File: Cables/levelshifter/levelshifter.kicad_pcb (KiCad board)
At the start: 2 copper layers, 40 x 18.5 mm, 55 parts, among them J1 DB25_Male, J10 Conn_01x01, J12 Conn_01x01, J13 Conn_01x01, J14 Conn_01x01, J15 Conn_01x01, J16 Conn_01x01, J17 Conn_01x01, J19 Conn_01x01, J2 Conn_01x01, J20 Conn_01x01, J21 Conn_01x01, J22 Conn_01x01, J23 Conn_01x01, J24 Conn_01x01, J25 Conn_01x01, J26 Conn_01x01, J27 Conn_01x01, J28 Conn_01x01, J29 Conn_01x01, J3 Conn_01x01, J4 Conn_01x01, J5 Conn_01x01, J6 Conn_01x01, J7 Conn_01x01, J9 Conn_01x01, U1 74AHCT1G126, U10 74AHCT1G125, U11 74AHCT1G125, U12 74AHCT1G125, U13 74AHCT1G125, U14 74AHCT1G126, U15 74AHCT1G126, U16 74AHCT1G126, U17 74AHCT1G126, U18 74AHCT1G126, U19 74AHCT1G126, U2 74AHCT1G126, U20 74AHCT1G126, U21 74AHCT1G125, U22 74AHCT1G125, U23 74AHCT1G125, U24 74AHCT1G125, U25 74AHCT1G125, U26 74AHCT1G125, U27 74AHCT1G126, U28 74AHCT1G125, U3 74AHCT1G126, U4 74AHCT1G126, U5 74AHCT1G126, U6 74AHCT1G126, U7 74AHCT1G126, U8 74AHCT1G125, U9 74AHCT1G125

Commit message: Tweak PT & LS PCBs
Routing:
- net /VOUT: track 84.6 -> 85.3 mm
- net /GND: vias 33 -> 34

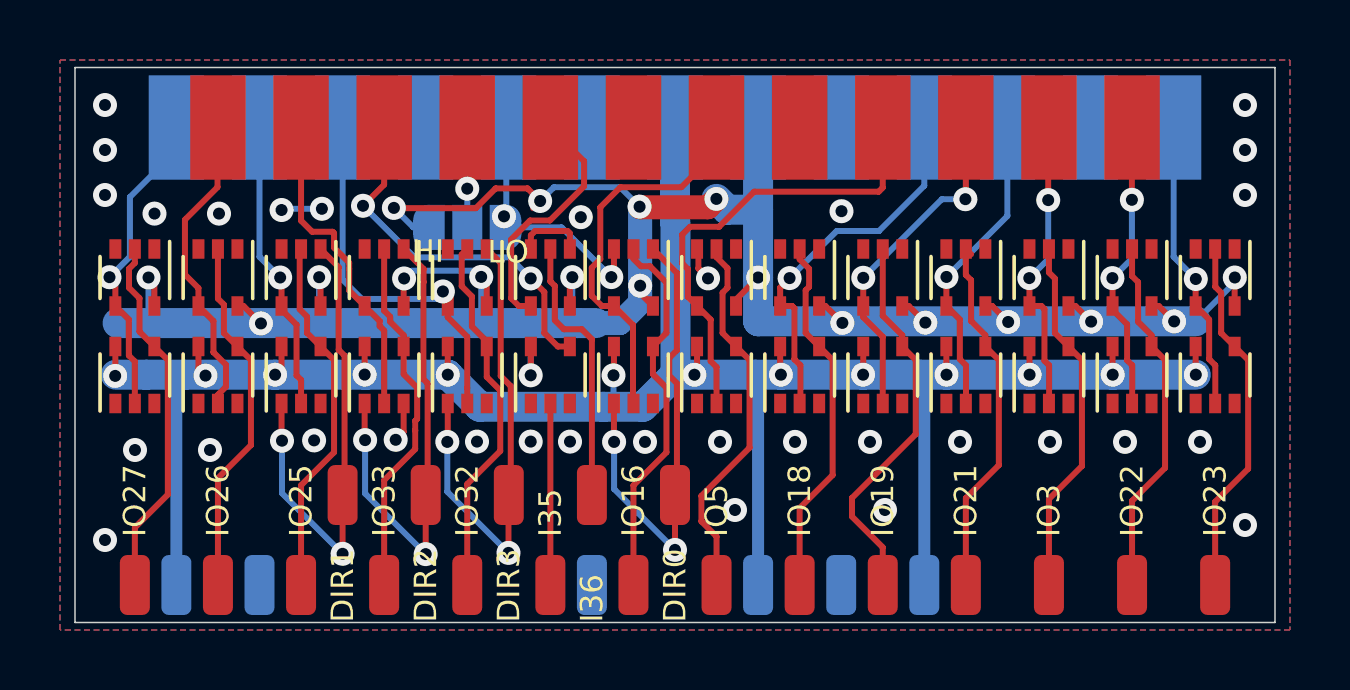
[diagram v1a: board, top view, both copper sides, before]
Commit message: Fixup inverted DB25 for Level Shifter PCB
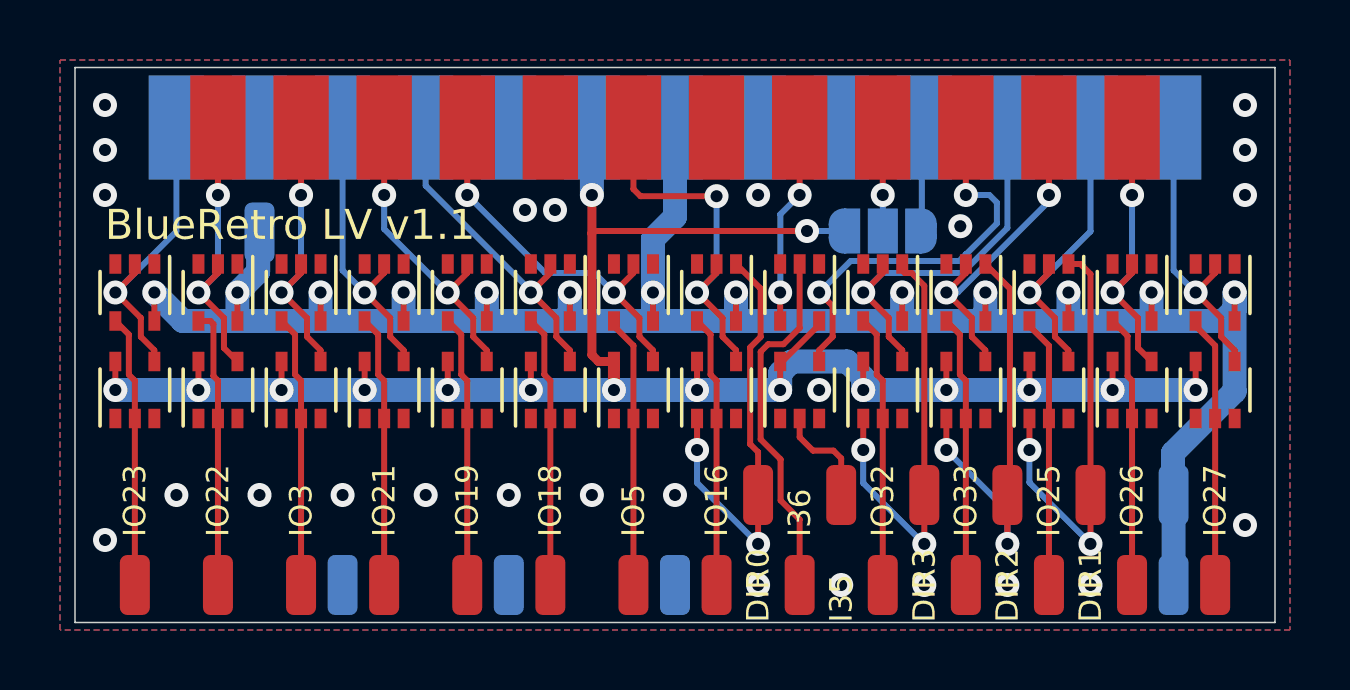
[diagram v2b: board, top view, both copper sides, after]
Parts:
- moved U1 36.2 mm to (-18.0, 1.50), turned to 90 degrees
- moved U18 36.2 mm to (18.0, 1.50), turned to 90 degrees
- moved U25 36.1 mm to (18.0, -1.75), turned to 270 degrees
- moved U8 36.1 mm to (-18.0, -1.75), turned to 270 degrees
- moved J29 36.0 mm to (18.0, 8.00)
- moved J9 36.0 mm to (-18.0, 8.00)
- moved J6 33.2 mm to (16.6, 8.00)
- moved U17 30.7 mm to (15.2, 1.50), turned to 90 degrees
- moved U2 30.7 mm to (-15.2, 1.50), turned to 90 degrees
- moved U24 30.6 mm to (15.2, -1.75), turned to 270 degrees
- moved U9 30.6 mm to (-15.2, -1.75), turned to 270 degrees
- moved J10 30.5 mm to (-15.2, 8.00)
- moved J28 30.5 mm to (15.2, 8.00)
- moved U15 25.2 mm to (12.5, 1.50), turned to 90 degrees
- moved U3 25.2 mm to (-12.5, 1.50), turned to 90 degrees
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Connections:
- J1 pad 1: /IO27 -> /IO23
- J1 pad 10: /IO18 -> /GND
- J1 pad 11: /IO21 -> /IO32
- J1 pad 12: (no net) -> /IO25
- J1 pad 13: /IO23 -> /IO27
- J1 pad 14: /IO26 -> /IO22
- J1 pad 15: /IO33 -> /IO3
- J1 pad 16: /I35 -> /IO19
- J1 pad 17: /I39 -> /IO5
- J1 pad 18: /I36 -> (no net)
- J1 pad 19: (no net) -> /IO16
- J1 pad 2: /IO25 -> (no net)
- J1 pad 20: /IO16 -> (no net)
- J1 pad 21: (no net) -> /I36
- J1 pad 22: /IO5 -> /I39
- J1 pad 23: /IO19 -> /I35
- J1 pad 24: /IO3 -> /IO33
- J1 pad 25: /IO22 -> /IO26
- J1 pad 3: /IO32 -> /IO21
- J1 pad 4: (no net) -> /IO18
- J1 pad 6: /GND -> /VOUT
- J1 pad 8: /VOUT -> /GND
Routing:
- net /VOUT: track 85.3 -> 69.4 mm, vias 19 -> 16
- net /GND: track 15.0 -> 3.49 mm, vias 34 -> 25
- net /IO19_C: track 13.0 -> 9.07 mm
- net /IO16_C: track 12.7 -> 9.07 mm
- net /IO5_C: track 12.7 -> 9.07 mm
- net /IO21_C: track 12.4 -> 9.07 mm
- net /IO27_C: track 12.3 -> 9.07 mm
- net /IO32_C: track 12.3 -> 9.07 mm
- net /IO18_C: track 12.2 -> 9.07 mm
- net /IO25_C: track 12.1 -> 9.07 mm
- net /IO33_C: track 12.1 -> 9.07 mm
- net /IO23_C: track 12.1 -> 9.07 mm
- net /IO3_C: track 12.1 -> 9.07 mm
- net /IO26_C: track 12.1 -> 9.07 mm
- net /I36_C: track 9.13 -> 12.1 mm
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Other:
- board text added: "BlueRetro LV v1.1"
- board text removed: "BlueRetro LV v1.0"

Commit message: Final tweak for JVS & LS PCBs
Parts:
- added J8: Conn_01x01, levelshifter:SolderWirePad_1x01_SMD_1x2mm, F.Cu at (16.6, 5.00)
- moved J6 3.30 mm to (15.2, 5.00)
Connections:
- U18 pad 1: /GND -> /DIR4
- U25 pad 1: /GND -> /DIR4
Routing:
- net /DIR4: track 0.00 -> 12.9 mm
- net /VIN: track 79.1 -> 77.5 mm
- net /GND: vias 25 -> 27
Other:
- board text added: "BlueRetro LS v1.1"
- board text added: "DIR4"
- board text removed: "BlueRetro LV v1.1"

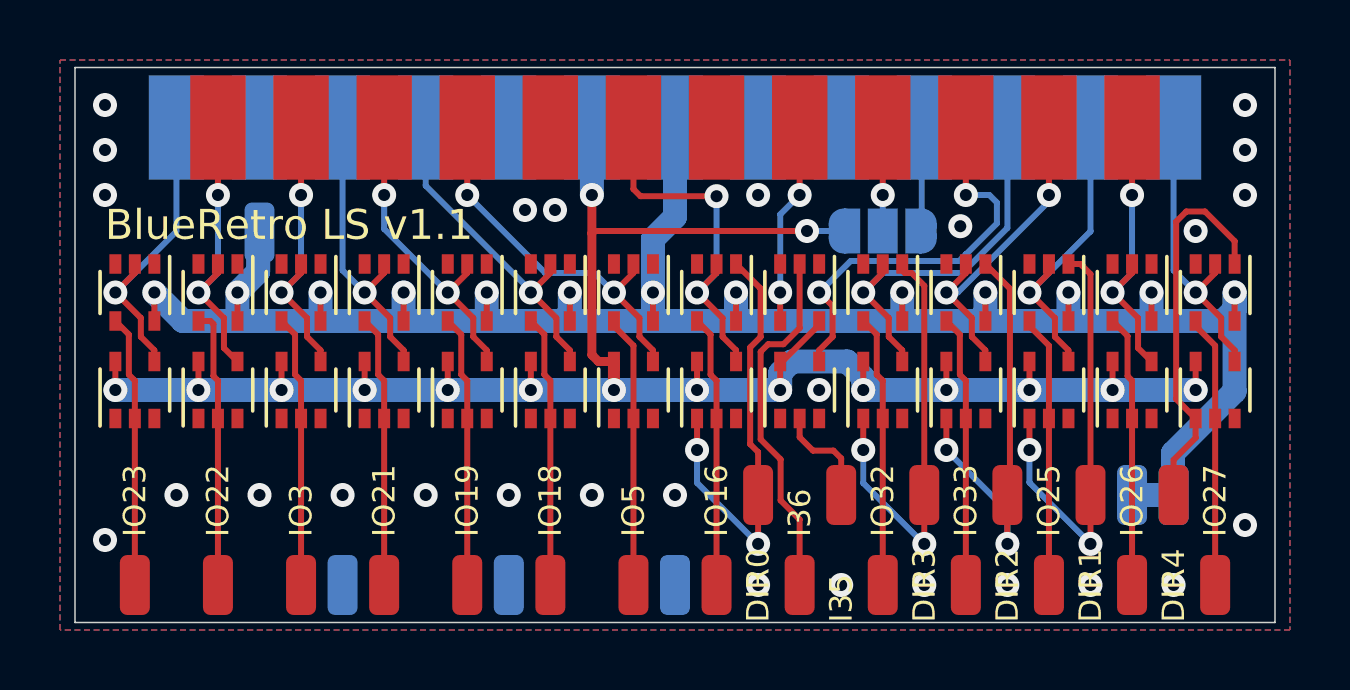
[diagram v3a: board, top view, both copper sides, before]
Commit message: [LS] Rework GND and VOUT supplies
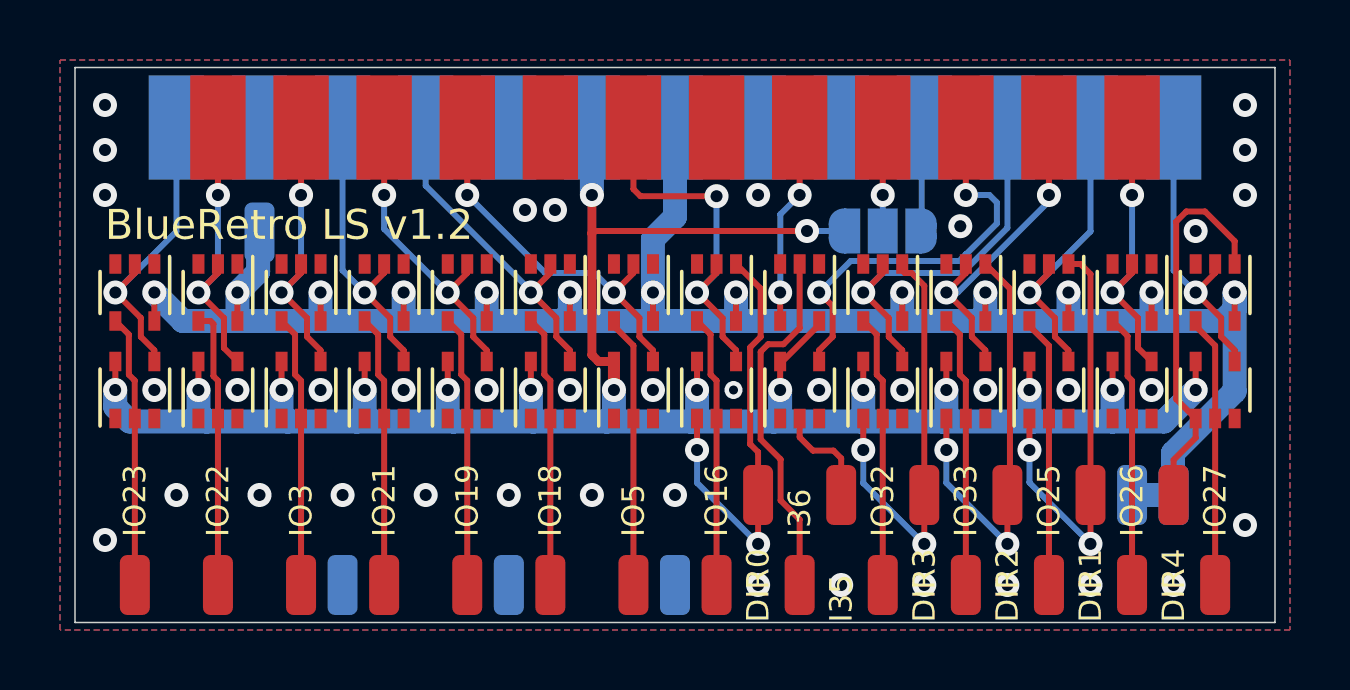
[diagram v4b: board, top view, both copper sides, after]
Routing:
- net /VOUT: track 69.4 -> 82.7 mm
- net /GND: vias 27 -> 39
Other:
- rule trace_min: 0.2 -> 0.15
- board text added: "BlueRetro LS v1.2"
- board text removed: "BlueRetro LS v1.1"

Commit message: [LS] Add pull-up footprint on 5V side for PAL NES & SNES cables
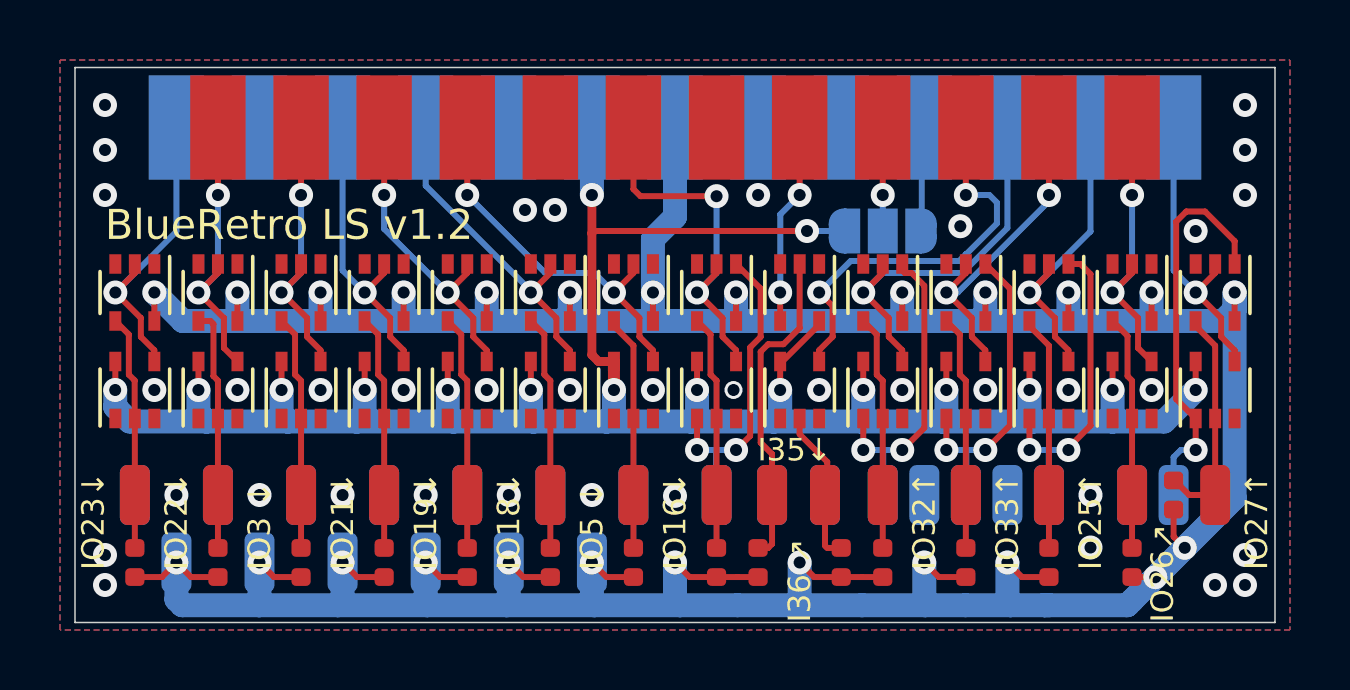
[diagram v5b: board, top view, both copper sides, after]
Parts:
- removed J20, J6, J7: Conn_01x01, levelshifter:SolderWirePad_1x01_SMD_1x2mm
- added J11: Conn_01x01, levelshifter:SolderWirePad_1x01_SMD_1x2mm, B.Cu at (-5.54, 7.25)
- added J18: Conn_01x01, levelshifter:SolderWirePad_1x01_SMD_1x2mm, B.Cu at (-15.2, 5.00)
- added J30: Conn_01x01, levelshifter:SolderWirePad_1x01_SMD_1x2mm, B.Cu at (-13.8, 7.25)
- added J31: Conn_01x01, levelshifter:SolderWirePad_1x01_SMD_1x2mm, B.Cu at (-9.70, 5.00)
- added J32: Conn_01x01, levelshifter:SolderWirePad_1x01_SMD_1x2mm, B.Cu at (-8.31, 7.25)
- added J33: Conn_01x01, levelshifter:SolderWirePad_1x01_SMD_1x2mm, B.Cu at (-6.92, 5.00)
- added J34: Conn_01x01, levelshifter:SolderWirePad_1x01_SMD_1x2mm, B.Cu at (-11.1, 7.25)
- added J35: Conn_01x01, levelshifter:SolderWirePad_1x01_SMD_1x2mm, B.Cu at (-18.0, 5.00)
- added J37: Conn_01x01, levelshifter:SolderWirePad_1x01_SMD_1x2mm, B.Cu at (-4.16, 5.00)
- added J38: Conn_01x01, levelshifter:SolderWirePad_1x01_SMD_1x2mm, B.Cu at (-16.6, 7.25)
- added J39: Conn_01x01, levelshifter:SolderWirePad_1x01_SMD_1x2mm, B.Cu at (-12.5, 5.00)
- added J40: Conn_01x01, levelshifter:SolderWirePad_1x01_SMD_1x2mm, B.Cu at (-2.77, 7.25)
- added J41: Conn_01x01, levelshifter:SolderWirePad_1x01_SMD_1x2mm, B.Cu at (-1.39, 5.00)
- added J42: Conn_01x01, levelshifter:SolderWirePad_1x01_SMD_1x2mm, B.Cu at (8.31, 5.00)
- added J43: Conn_01x01, levelshifter:SolderWirePad_1x01_SMD_1x2mm, B.Cu at (11.1, 5.00)
- added R1: DNP, levelshifter:R_0402_1005Metric, F.Cu at (-18.0, 7.25)
- added R10: DNP, levelshifter:R_0402_1005Metric, F.Cu at (5.54, 7.25)
- added R11: DNP, levelshifter:R_0402_1005Metric, F.Cu at (6.92, 7.25)
- added R12: DNP, levelshifter:R_0402_1005Metric, F.Cu at (9.70, 7.25)
- added R13: DNP, levelshifter:R_0402_1005Metric, F.Cu at (12.5, 7.25)
- added R14: DNP, levelshifter:R_0402_1005Metric, F.Cu at (15.2, 7.25)
- added R15: DNP, levelshifter:R_0402_1005Metric, F.Cu at (16.6, 5.00)
- added R2: DNP, levelshifter:R_0402_1005Metric, F.Cu at (-15.2, 7.25)
- added R3: DNP, levelshifter:R_0402_1005Metric, F.Cu at (-12.5, 7.25)
- added R4: DNP, levelshifter:R_0402_1005Metric, F.Cu at (-9.70, 7.25)
- added R5: DNP, levelshifter:R_0402_1005Metric, F.Cu at (-6.92, 7.25)
- added R6: DNP, levelshifter:R_0402_1005Metric, F.Cu at (-4.16, 7.25)
- added R7: DNP, levelshifter:R_0402_1005Metric, F.Cu at (-1.39, 7.25)
- added R8: DNP, levelshifter:R_0402_1005Metric, F.Cu at (1.39, 7.25)
- added R9: DNP, levelshifter:R_0402_1005Metric, F.Cu at (2.77, 7.25)
- J2, J3, J4, J5, J8: moved to B.Cu
- moved J21 15.5 mm to (15.2, 5.00)
- moved J17 14.6 mm to (3.23, 5.00)
- moved J23 11.0 mm to (5.00, 5.00)
- moved J22 3.14 mm to (3.23, 5.00)
- moved J10 3.00 mm to (-15.2, 5.00)
- moved J12 3.00 mm to (-12.5, 5.00)
- moved J13 3.00 mm to (-9.70, 5.00)
- moved J14 3.00 mm to (-6.92, 5.00)
- moved J15 3.00 mm to (-4.16, 5.00)
- moved J16 3.00 mm to (-1.39, 5.00)
- moved J19 3.00 mm to (1.39, 5.00)
- moved J25 3.00 mm to (6.92, 5.00)
- moved J26 3.00 mm to (9.70, 5.00)
- moved J27 3.00 mm to (12.5, 5.00)
- moved J28 3.00 mm to (15.2, 5.00)
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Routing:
- net /VIN: track 77.5 -> 146.9 mm, vias 13 -> 25
- net /DIR0: track 14.9 -> 10.7 mm
- net /DIR3: track 14.8 -> 10.8 mm
- net /DIR2: track 14.7 -> 10.7 mm
- net /DIR1: track 14.9 -> 10.9 mm
- net /I35_C: track 3.52 -> 5.19 mm
- net /IO27_C: track 9.07 -> 7.66 mm
- net /IO26_C: track 9.07 -> 7.83 mm
- net /IO32_C: track 9.07 -> 7.83 mm
- net /IO23_C: track 9.07 -> 7.83 mm
- net /IO22_C: track 9.30 -> 8.07 mm
- net /IO18_C: track 9.07 -> 7.83 mm
- net /IO5_C: track 9.07 -> 7.83 mm
- net /IO3_C: track 9.07 -> 7.83 mm
- net /IO33_C: track 9.07 -> 7.83 mm
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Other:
- board text added: "GND→"
- board text added: "I35↓"
- board text added: "I36 ↗"
- board text added: "IO16↓"
- board text added: "IO18↓"
- board text added: "IO19↓"
- board text added: "IO21↓"
- board text added: "IO22↓"
- board text added: "IO23↓"
- board text added: "IO25↑"
- board text added: "IO26↗"
- board text added: "IO27↑"
- board text added: "IO3 ↓"
- board text added: "IO32↑"
- board text added: "IO33↑"
- board text added: "IO5 ↓"
- board text added: "←VIN"
- board text removed: "GND"
- board text removed: "I35"
- board text removed: "I36"
- board text removed: "IO16"
- board text removed: "IO18"
- board text removed: "IO19"
- board text removed: "IO21"
- board text removed: "IO22"
- board text removed: "IO23"
- board text removed: "IO25"
- board text removed: "IO26"
- board text removed: "IO27"
- board text removed: "IO3"
- board text removed: "IO32"
- board text removed: "IO33"
- board text removed: "IO5"
- board text removed: "VIN"
